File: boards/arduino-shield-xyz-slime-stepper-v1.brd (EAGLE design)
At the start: 73.7 x 55.5 mm, 27 parts, among them IC1 2967-MP6500, IC3 2967-MP6500, J4 ARDUINO_R3_SHIELD, J9 455-1750-1-ND

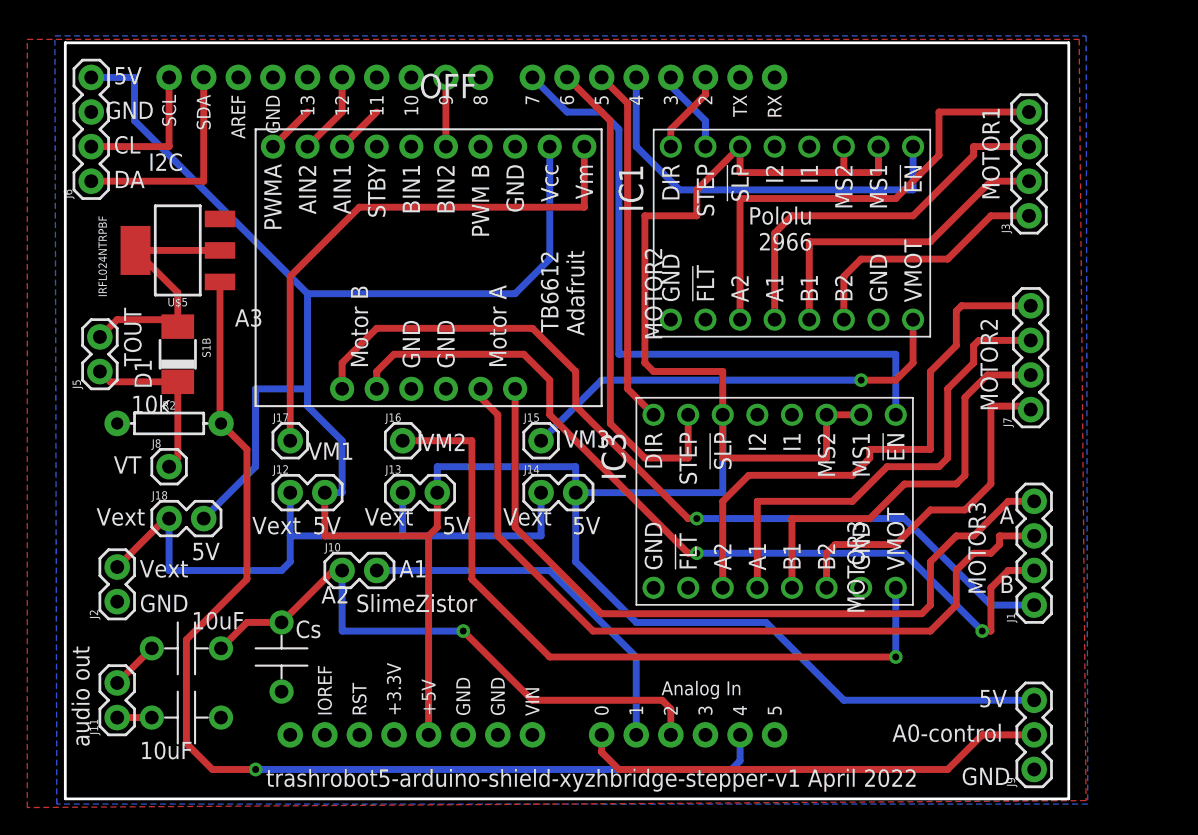
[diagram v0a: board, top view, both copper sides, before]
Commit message: two new boards, xyz and slime and xyzhbridge and slime
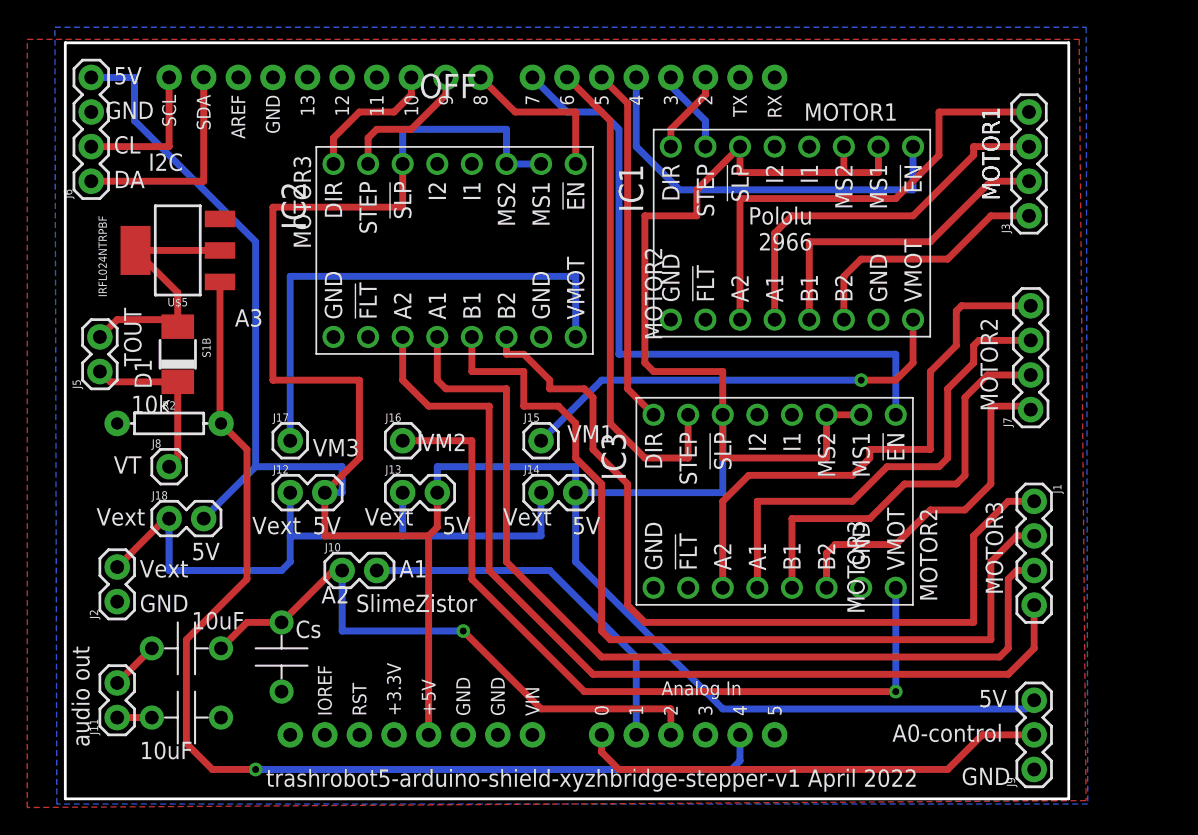
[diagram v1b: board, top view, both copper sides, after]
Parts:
- removed U$1: ADAFRUIT-TB6612, spietz-library-2:ADAFRUIT-TB6612
- added IC2: 2967-MP6500, pololu-stepper-driver:MP6500
- moved J1 7.62 mm to (73.7, 22.2), turned to 270 degrees
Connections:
- removed net AIN1: J4.D13, U$1.AIN1
- removed net AIN2: J4.D12, U$1.AIN2
- removed net BIN1: J4.D8, U$1.BIN1
- removed net BIN2: J4.D9, U$1.BIN2
- removed net N$17: J1.3, U$1.MA2
- removed net PWMA: J4.D11, U$1.PWMA
- removed net PWMB: J4.D10, U$1.PWMB
- removed net STBY: U$1.STBY
- new net DIR3: IC2.8, J4.D10
- new net EN3: IC2.1, J4.D8
- new net N$10: IC2.14, J1.1
- new net STEP3: IC2.7, J4.D9
- net 5V: now also IC2.2, IC2.3, IC2.6; no longer U$1.VCC
- net GND: now also IC2.15, IC2.9; no longer U$1.G2, U$1.G3, U$1.GND
- net N$11: now also IC2.13; no longer U$1.MB1
- net N$12: now also IC2.12, J1.3; no longer J1.1, U$1.MB2
- net N$16: now also IC2.11; no longer U$1.MA1
- net VMOT3: now also IC2.16; no longer U$1.VM
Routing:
- net N$10: track 0.00 -> 63.4 mm
- net N$17: track 58.3 -> 0.00 mm
- net 5V: track 248.0 -> 272.0 mm
- net N$16: track 56.2 -> 70.1 mm
- net EN3: track 0.00 -> 11.8 mm
- net STEP3: track 0.00 -> 10.2 mm
- net DIR3: track 0.00 -> 10.2 mm
- net AIN2: track 6.13 -> 0.00 mm
- net BIN2: track 5.08 -> 0.00 mm
- net N$12: track 63.7 -> 68.5 mm, vias 1 -> 0
- net N$11: track 63.7 -> 67.8 mm, vias 2 -> 0
- net PWMA: track 3.59 -> 0.00 mm
- net AIN1: track 3.59 -> 0.00 mm
- net VMOT2: track 53.8 -> 57.4 mm
- net VMOT3: track 40.2 -> 37.5 mm
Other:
- board text removed: "A"
- board text removed: "B"
